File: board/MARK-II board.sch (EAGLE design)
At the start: 168 parts, among them IC1 MAX3243CPWR, IC10 IFX1963TBV, IC11 IFX1963TBV, IC12 ATTINY441-SSU, IC13 LD1117S33, IC2 FT230XS, IC3 ENC28J60SS, IC4 PCM5100, IC5 IS42S83200, IC6 MCP7940NSN, IC7 FM24CL16BG, IC8 AT25DN256SS, IC9 10M25SAE144, Q1 25MHz, Q2 32.768kHz, Q3 CMI-1275C-050, Q4 25MHz, Q5 18,432MHz, Q6 22.5792MHz, T1 BC337-16 A1, X1 MINI-USBUX60A-MB-5ST, X10 T821-106A1S100, X11 T821-110A1S100, X12 PJ-002BH-SMT-TR, X13 T821-106A1S100, X2 L717SDE09P1ACH4F, X3 L77HDE15SD1CH4R, X4 MD-60SM, X5 RB1-125BAG1A, X6 SJ1-3535NG, X7 MICROSD-HRS_DM3D, X8 BAT-HLD-002-SMT, X9 T821-120A1S100

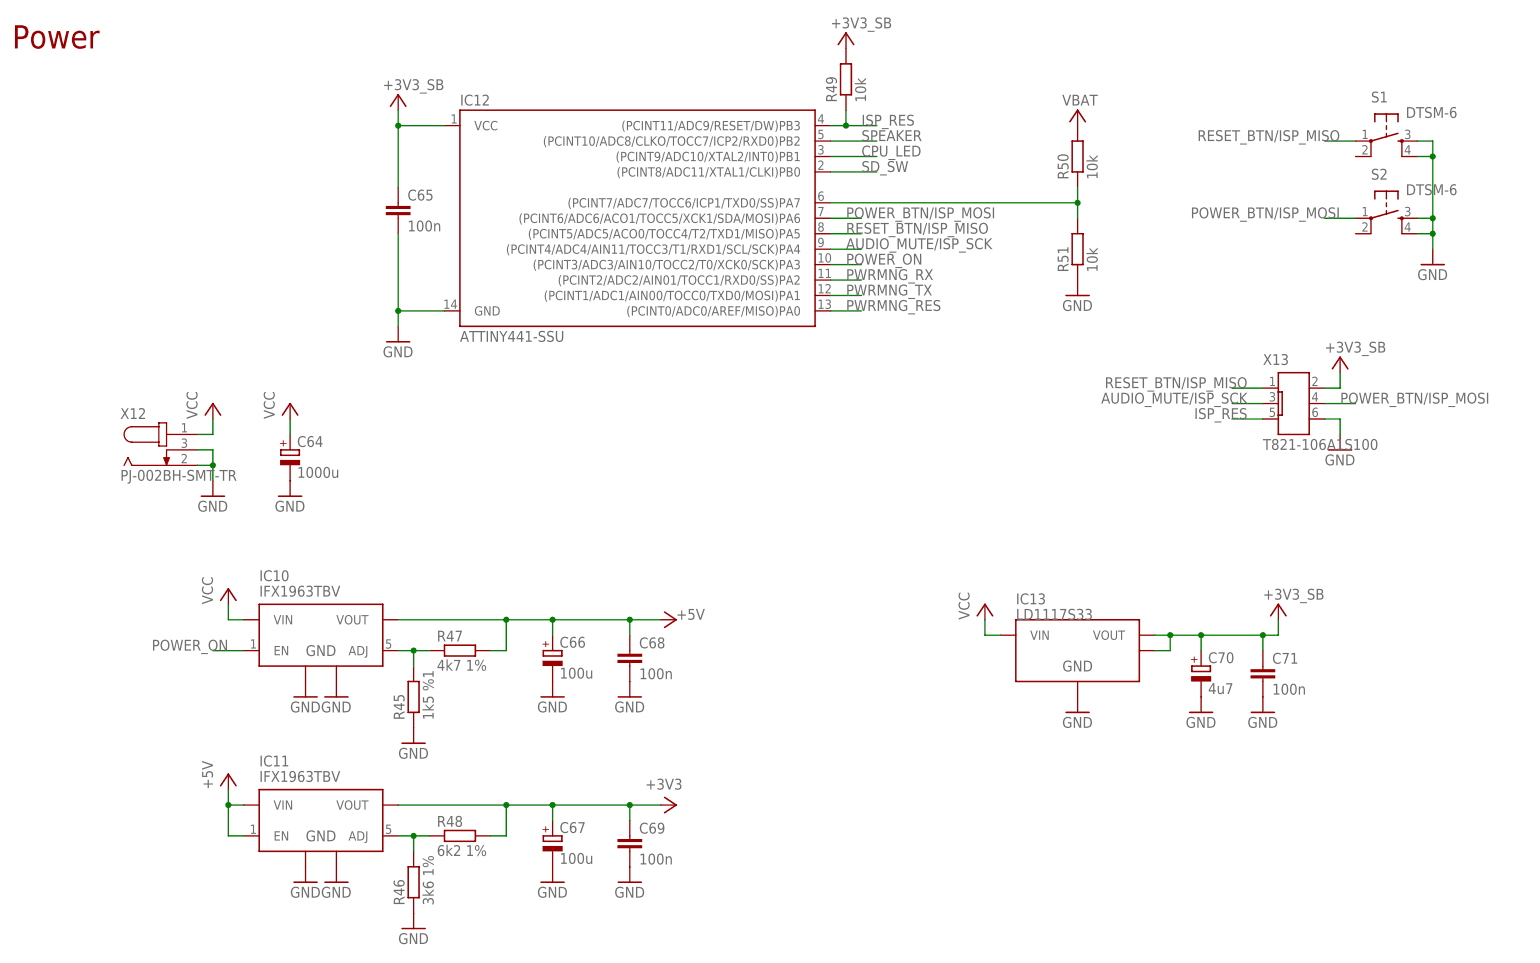
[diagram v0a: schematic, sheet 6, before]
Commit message: power mng IC changet to Atmega48PB
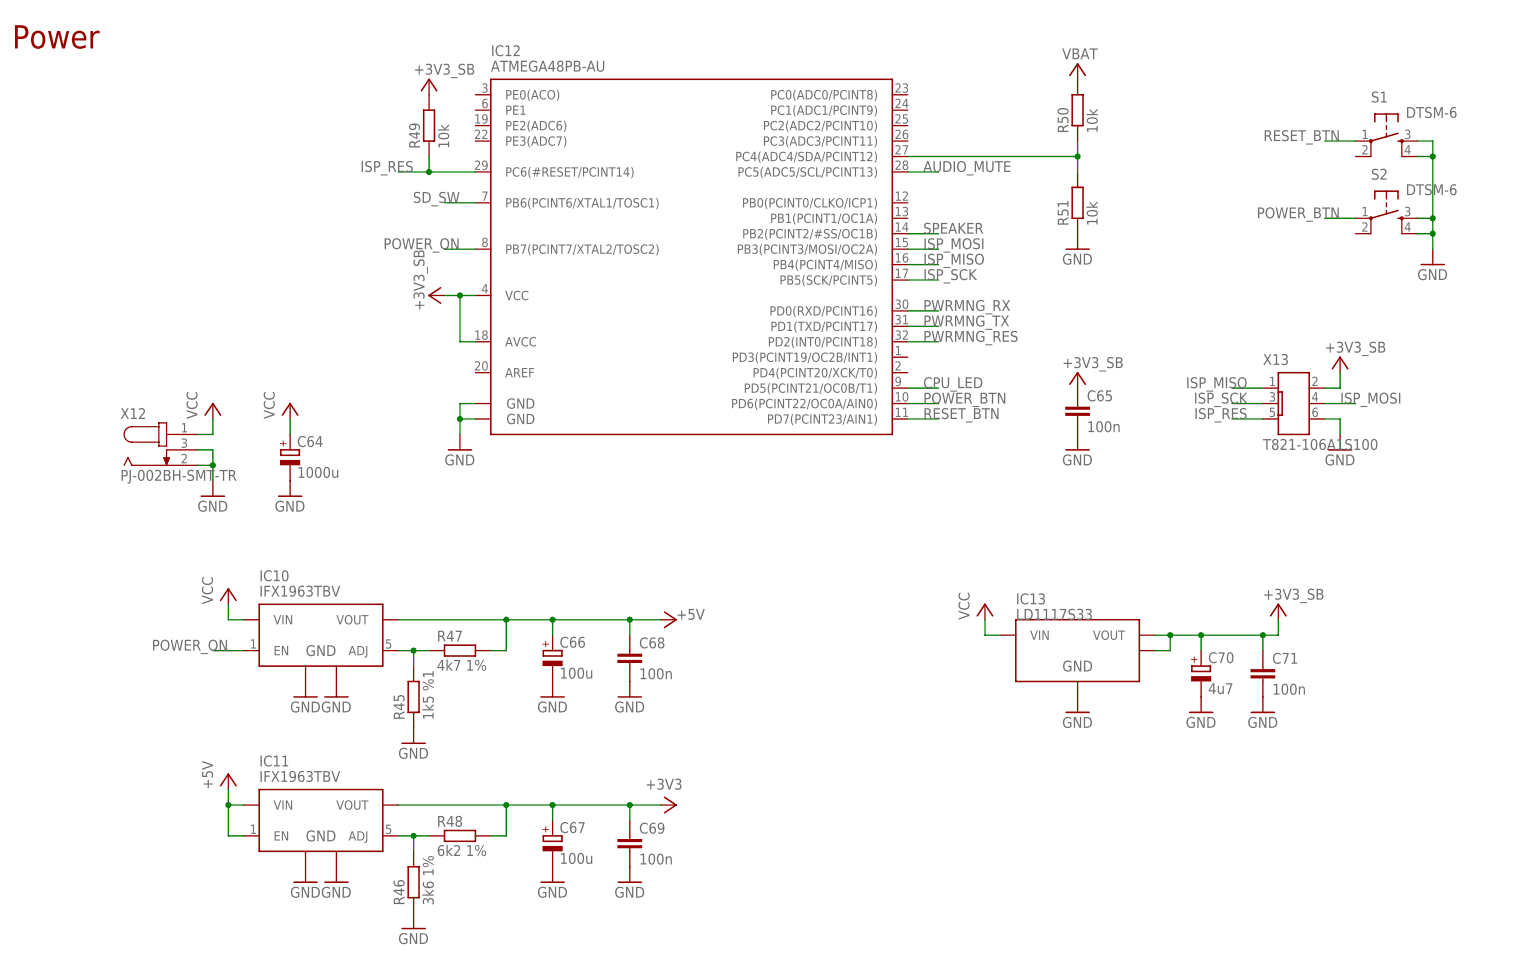
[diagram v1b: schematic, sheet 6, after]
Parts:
- IC12: value ATTINY441-SSU -> ATMEGA48PB-AU; device ic:ATTINY441-SSU -> ic:ATMEGA48PB-AU; MOUSER 556-ATTINY441-SSU -> 556-ATMEGA48PB-AU
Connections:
- removed net AUDIO_MUTE/ISP_SCK: IC12.(PCINT4/ADC4/AIN11/TOCC3/T1/RXD1/SCL/SCK)PA4, IC4_IO.XSMT, X13.3
- removed net POWER_BTN/ISP_MOSI: IC12.(PCINT6/ADC6/ACO1/TOCC5/XCK1/SDA/MOSI)PA6, S2.1, X10.4, X13.4
- removed net RESET_BTN/ISP_MISO: IC12.(PCINT5/ADC5/ACO0/TOCC4/T2/TXD1/MISO)PA5, S1.1, X10.2, X13.1
- new net AUDIO_MUTE: IC12.PC5(ADC5/SCL/PCINT13), IC4_IO.XSMT
- new net ISP_MISO: IC12.PB4(PCINT4/MISO), X13.1
- new net ISP_MOSI: IC12.PB3(PCINT3/MOSI/OC2A), X13.4
- new net ISP_SCK: IC12.PB5(SCK/PCINT5), X13.3
- new net POWER_BTN: IC12.PD6(PCINT22/OC0A/AIN0), S2.1, X10.4
- new net RESET_BTN: IC12.PD7(PCINT23/AIN1), S1.1, X10.2
- net +3V3_SB: now also IC12.AVCC
- net CPU_LED: now also IC12.PD5(PCINT21/OC0B/T1); no longer IC12.(PCINT9/ADC10/XTAL2/INT0)PB1
- net GND: now also IC12.GND@1, IC12.GND@2; no longer IC12.GND
- net ISP_RES: now also IC12.PC6(#RESET/PCINT14); no longer IC12.(PCINT11/ADC9/RESET/DW)PB3
- net N$21: now also IC12.PC4(ADC4/SDA/PCINT12); no longer IC12.(PCINT7/ADC7/TOCC6/ICP1/TXD0/SS)PA7
- net POWER_ON: now also IC12.PB7(PCINT7/XTAL2/TOSC2); no longer IC12.(PCINT3/ADC3/AIN10/TOCC2/T0/XCK0/SCK)PA3
- net PWRMNG_RES: now also IC12.PD2(INT0/PCINT18); no longer IC12.(PCINT0/ADC0/AREF/MISO)PA0
- net PWRMNG_RX: now also IC12.PD0(RXD/PCINT16); no longer IC12.(PCINT2/ADC2/AIN01/TOCC1/RXD0/SS)PA2
- net PWRMNG_TX: now also IC12.PD1(TXD/PCINT17); no longer IC12.(PCINT1/ADC1/AIN00/TOCC0/TXD0/MOSI)PA1
- net SD_SW: now also IC12.PB6(PCINT6/XTAL1/TOSC1); no longer IC12.(PCINT8/ADC11/XTAL1/CLKI)PB0
- net SPEAKER: now also IC12.PB2(PCINT2/#SS/OC1B); no longer IC12.(PCINT10/ADC8/CLKO/TOCC7/ICP2/RXD0)PB2
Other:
- moved on the sheet: C65, R49, R50, R51

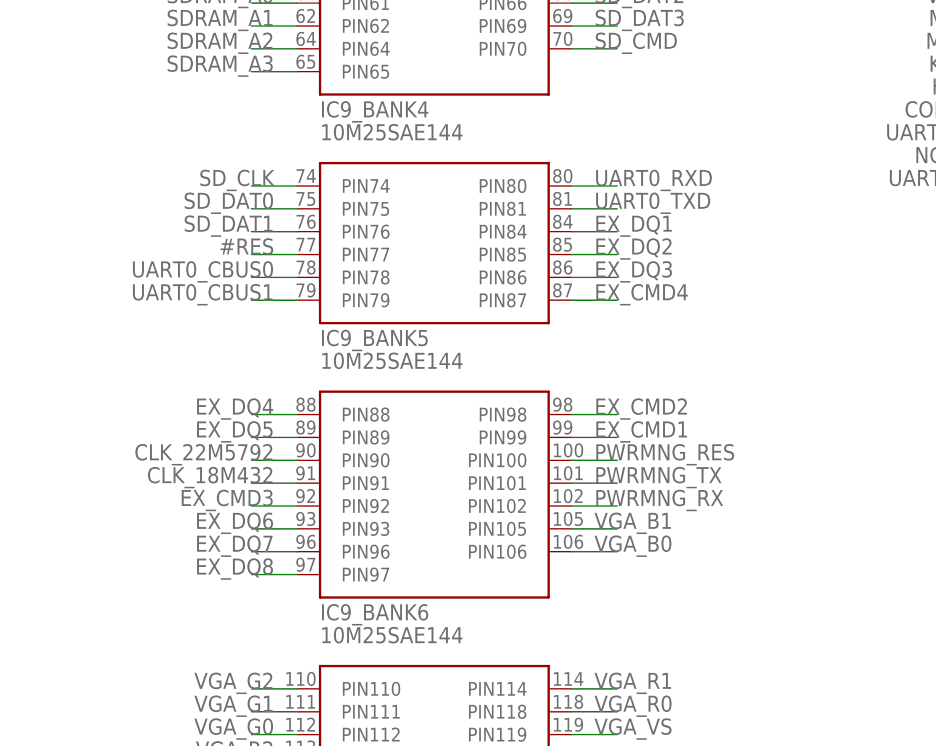
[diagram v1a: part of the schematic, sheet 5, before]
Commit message: Small name changes to better suits HDL files
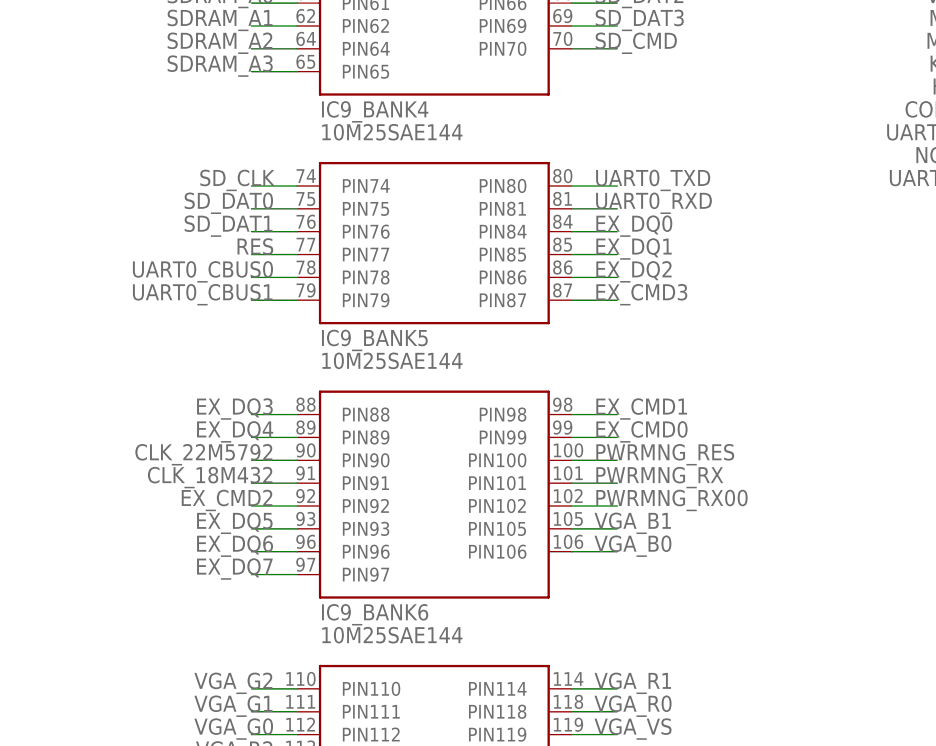
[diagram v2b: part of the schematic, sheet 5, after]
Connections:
- net #RES renamed RES
- removed net EX_CMD4: IC9_BANK5.PIN87, X9-15.KL
- removed net EX_DQ8: IC9_BANK6.PIN97, X9-5.KL
- new net EX_CMD0: IC9_BANK6.PIN99, X9-1.KL
- new net EX_DQ0: IC9_BANK5.PIN84, X9-19.KL
- new net PWRMNG_RX00: IC9_BANK6.PIN102
- net EX_CMD1: now also IC9_BANK6.PIN98, X9-3.KL; no longer IC9_BANK6.PIN99, X9-1.KL
- net EX_CMD2: now also IC9_BANK6.PIN92, X9-11.KL; no longer IC9_BANK6.PIN98, X9-3.KL
- net EX_CMD3: now also IC9_BANK5.PIN87, X9-15.KL; no longer IC9_BANK6.PIN92, X9-11.KL
- net EX_DQ1: now also IC9_BANK5.PIN85, X9-17.KL; no longer IC9_BANK5.PIN84, X9-19.KL
- net EX_DQ2: now also IC9_BANK5.PIN86, X9-16.KL; no longer IC9_BANK5.PIN85, X9-17.KL
- net EX_DQ3: now also IC9_BANK6.PIN88, X9-14.KL; no longer IC9_BANK5.PIN86, X9-16.KL
- net EX_DQ4: now also IC9_BANK6.PIN89, X9-12.KL; no longer IC9_BANK6.PIN88, X9-14.KL
- net EX_DQ5: now also IC9_BANK6.PIN93, X9-10.KL; no longer IC9_BANK6.PIN89, X9-12.KL
- net EX_DQ6: now also IC9_BANK6.PIN96, X9-8.KL; no longer IC9_BANK6.PIN93, X9-10.KL
- net EX_DQ7: now also IC9_BANK6.PIN97, X9-5.KL; no longer IC9_BANK6.PIN96, X9-8.KL
- net PWRMNG_RX: now also IC12.PD1(TXD/PCINT17), IC9_BANK6.PIN101; no longer IC12.PD0(RXD/PCINT16), IC9_BANK6.PIN102
- net PWRMNG_TX: now also IC12.PD0(RXD/PCINT16); no longer IC12.PD1(TXD/PCINT17), IC9_BANK6.PIN101
- net UART0_RXD: now also IC2.TXD, IC9_BANK5.PIN81; no longer IC2.RXD, IC9_BANK5.PIN80
- net UART0_TXD: now also IC2.RXD, IC9_BANK5.PIN80; no longer IC2.TXD, IC9_BANK5.PIN81
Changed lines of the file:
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@@
 </segment>
 </net>
-<net name="UART0_TXD" class="2">
+<net name="UART0_RXD" class="2">
 <segment>
 <pinref part="IC2" gate="G$2" pin="TXD"/>
@@
 </segment>
 </net>
-<net name="UART0_RXD" class="2">
+<net name="UART0_TXD" class="2">
 <segment>
 <pinref part="IC2" gate="G$2" pin="RXD"/>
@@
 </segment>
 </net>
-<net name="#RES" class="2">
+<net name="RES" class="2">
 <segment>
 <pinref part="IC3" gate="G$1" pin="!RESET"/>
@@
 </segment>
 </net>
-<net name="EX_DQ1" class="2">
+<net name="EX_DQ0" class="2">
 <segment>
 <wire x1="116.84" y1="99.06" x2="132.08" y2="99.06" width="0.1524" layer="91"/>
@@
 </segment>
 </net>
-<net name="EX_DQ2" class="2">
+<net name="EX_DQ1" class="2">
 <segment>
 <wire x1="116.84" y1="104.14" x2="132.08" y2="104.14" width="0.1524" layer="91"/>
@@
 </segment>
 </net>
-<net name="EX_DQ4" class="2">
+<net name="EX_DQ3" class="2">
 <segment>
 <wire x1="116.84" y1="111.76" x2="132.08" y2="111.76" width="0.1524" layer="91"/>
@@
 </segment>
 </net>
-<net name="EX_DQ5" class="2">
+<net name="EX_DQ4" class="2">
 <segment>
 <wire x1="116.84" y1="116.84" x2="132.08" y2="116.84" width="0.1524" layer="91"/>
@@
 </segment>
 </net>
-<net name="EX_DQ6" class="2">
+<net name="EX_DQ5" class="2">
 <segment>
 <wire x1="116.84" y1="121.92" x2="132.08" y2="121.92" width="0.1524" layer="91"/>
@@
 </segment>
 </net>
-<net name="EX_DQ7" class="2">
+<net name="EX_DQ6" class="2">
 <segment>
 <wire x1="116.84" y1="127" x2="132.08" y2="127" width="0.1524" layer="91"/>
@@
 </segment>
 </net>
-<net name="EX_DQ8" class="2">
+<net name="EX_DQ7" class="2">
 <segment>
 <wire x1="116.84" y1="134.62" x2="132.08" y2="134.62" width="0.1524" layer="91"/>
@@
 </segment>
 </net>
-<net name="EX_DQ3" class="2">
+<net name="EX_DQ2" class="2">
 <segment>
 <wire x1="116.84" y1="106.68" x2="132.08" y2="106.68" width="0.1524" layer="91"/>
@@
 </segment>
 </net>
-<net name="EX_CMD1" class="2">
+<net name="EX_CMD0" class="2">
 <segment>
 <wire x1="116.84" y1="144.78" x2="132.08" y2="144.78" width="0.1524" layer="91"/>
@@
 </segment>
 </net>
-<net name="EX_CMD2" class="2">
+<net name="EX_CMD1" class="2">
 <segment>
 <wire x1="116.84" y1="139.7" x2="132.08" y2="139.7" width="0.1524" layer="91"/>
@@
 </segment>
 </net>
-<net name="EX_CMD4" class="2">
+<net name="EX_CMD3" class="2">
 <segment>
 <wire x1="116.84" y1="109.22" x2="132.08" y2="109.22" width="0.1524" layer="91"/>
@@
 </segment>
 </net>
-<net name="EX_CMD3" class="2">
+<net name="EX_CMD2" class="2">
 <segment>
 <wire x1="116.84" y1="119.38" x2="132.08" y2="119.38" width="0.1524" layer="91"/>
@@
 </segment>
 </net>
-<net name="#RES" class="2">
+<net name="RES" class="2">
 <segment>
 <wire x1="116.84" y1="129.54" x2="132.08" y2="129.54" width="0.1524" layer="91"/>
@@
 </segment>
 </net>
-<net name="EX_DQ1" class="2">
+<net name="EX_DQ0" class="2">
 <segment>
 <pinref part="IC9" gate="_BANK5" pin="PIN84"/>
@@
 </segment>
 </net>
-<net name="EX_DQ2" class="2">
+<net name="EX_DQ1" class="2">
 <segment>
 <pinref part="IC9" gate="_BANK5" pin="PIN85"/>
@@
 </segment>
 </net>
-<net name="EX_DQ3" class="2">
+<net name="EX_DQ2" class="2">
 <segment>
 <pinref part="IC9" gate="_BANK5" pin="PIN86"/>
@@
 </segment>
 </net>
-<net name="EX_CMD4" class="2">
+<net name="EX_CMD3" class="2">
 <segment>
 <pinref part="IC9" gate="_BANK5" pin="PIN87"/>
@@
 </segment>
 </net>
-<net name="EX_DQ4" class="2">
+<net name="EX_DQ3" class="2">
 <segment>
 <pinref part="IC9" gate="_BANK6" pin="PIN88"/>
@@
 </segment>
 </net>
-<net name="EX_DQ5" class="2">
+<net name="EX_DQ4" class="2">
 <segment>
 <pinref part="IC9" gate="_BANK6" pin="PIN89"/>
@@
 </segment>
 </net>
-<net name="EX_CMD3" class="2">
+<net name="EX_CMD2" class="2">
 <segment>
 <pinref part="IC9" gate="_BANK6" pin="PIN92"/>
@@
 </segment>
 </net>
-<net name="EX_DQ6" class="2">
+<net name="EX_DQ5" class="2">
 <segment>
 <pinref part="IC9" gate="_BANK6" pin="PIN93"/>
@@
 </segment>
 </net>
-<net name="EX_CMD2" class="2">
+<net name="EX_CMD1" class="2">
 <segment>
 <pinref part="IC9" gate="_BANK6" pin="PIN98"/>
@@
 </segment>
 </net>
-<net name="EX_CMD1" class="2">
+<net name="EX_CMD0" class="2">
 <segment>
 <pinref part="IC9" gate="_BANK6" pin="PIN99"/>
@@
 </segment>
 </net>
-<net name="EX_DQ8" class="2">
+<net name="EX_DQ7" class="2">
 <segment>
 <pinref part="IC9" gate="_BANK6" pin="PIN97"/>
@@
 </segment>
 </net>
-<net name="EX_DQ7" class="2">
+<net name="EX_DQ6" class="2">
 <segment>
 <pinref part="IC9" gate="_BANK6" pin="PIN96"/>
@@
 </segment>
 </net>
-<net name="UART0_TXD" class="2">
+<net name="UART0_RXD" class="2">
 <segment>
 <pinref part="IC9" gate="_BANK5" pin="PIN81"/>
@@
 </segment>
 </net>
-<net name="PWRMNG_RX" class="2">
+<net name="PWRMNG_RX00" class="2">
 <segment>
 <pinref part="IC9" gate="_BANK6" pin="PIN102"/>
@@
 </segment>
 </net>
-<net name="PWRMNG_TX" class="2">
+<net name="PWRMNG_RX" class="2">
 <segment>
 <pinref part="IC9" gate="_BANK6" pin="PIN101"/>
@@
 </segment>
 </net>
-<net name="#RES" class="2">
+<net name="RES" class="2">
 <segment>
 <pinref part="IC9" gate="_BANK5" pin="PIN77"/>
@@
 </segment>
 </net>
-<net name="UART0_RXD" class="2">
+<net name="UART0_TXD" class="2">
 <segment>
 <pinref part="IC9" gate="_BANK5" pin="PIN80"/>
@@
 </segment>
 </net>
-<net name="PWRMNG_TX" class="2">
+<net name="PWRMNG_RX" class="2">
 <segment>
 <pinref part="IC12" gate="G$1" pin="PD1(TXD/PCINT17)"/>
@@
 </segment>
 </net>
-<net name="PWRMNG_RX" class="2">
-<segment>
-<pinref part="IC12" gate="G$1" pin="PD0(RXD/PCINT16)"/>
-<wire x1="154.94" y1="124.46" x2="160.02" y2="124.46" width="0.1524" layer="91"/>
-<label x="157.48" y="124.46" size="1.778" layer="95"/>
-</segment>
-</net>
 <net name="PWRMNG_RES" class="2">
 <segment>
@@
 </segment>
 </net>
+<net name="PWRMNG_TX" class="2">
+<segment>
+<pinref part="IC12" gate="G$1" pin="PD0(RXD/PCINT16)"/>
+<wire x1="154.94" y1="124.46" x2="160.02" y2="124.46" width="0.1524" layer="91"/>
+<label x="157.48" y="124.46" size="1.778" layer="95"/>
+</segment>
+</net>

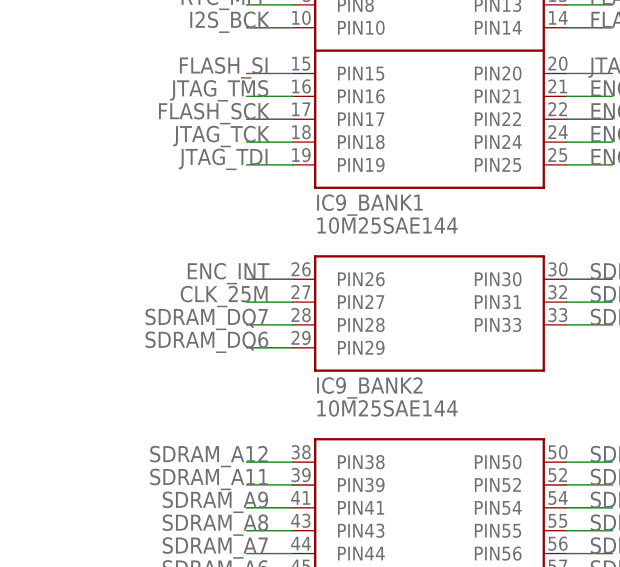
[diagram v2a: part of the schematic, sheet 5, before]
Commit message: Fix clk for pll
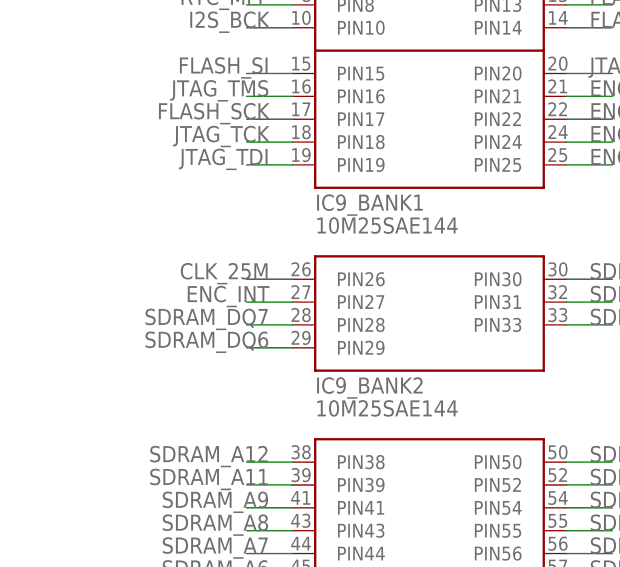
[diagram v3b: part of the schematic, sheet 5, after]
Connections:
- net CLK_25M: now also IC9_BANK2.PIN26; no longer IC9_BANK2.PIN27
- net ENC_INT: now also IC9_BANK2.PIN27; no longer IC9_BANK2.PIN26
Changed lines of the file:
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@@
 <net name="CLK_25M" class="2">
+<segment>
+<pinref part="IC9" gate="_BANK2" pin="PIN26"/>
+<wire x1="38.1" y1="129.54" x2="33.02" y2="129.54" width="0.1524" layer="91"/>
+<label x="35.56" y="129.54" size="1.778" layer="95" rot="MR0"/>
+</segment>
+</net>
+<net name="ENC_INT" class="2">
 <segment>
 <pinref part="IC9" gate="_BANK2" pin="PIN27"/>
@@
 </segment>
 </net>
-<net name="ENC_INT" class="2">
-<segment>
-<pinref part="IC9" gate="_BANK2" pin="PIN26"/>
-<wire x1="38.1" y1="129.54" x2="33.02" y2="129.54" width="0.1524" layer="91"/>
-<label x="35.56" y="129.54" size="1.778" layer="95" rot="MR0"/>
-</segment>
-</net>
